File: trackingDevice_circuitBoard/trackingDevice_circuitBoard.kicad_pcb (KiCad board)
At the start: 2 copper layers, 58.4 x 45.7 mm, 15 parts, among them P1 Digital, P4 Analog, Q1 2N7000, Q2 Q_NPN_EBC, Q3 Q_NPN_EBC, U1 HC-12, U2 GY-NEO6MV2, U3 TP4056

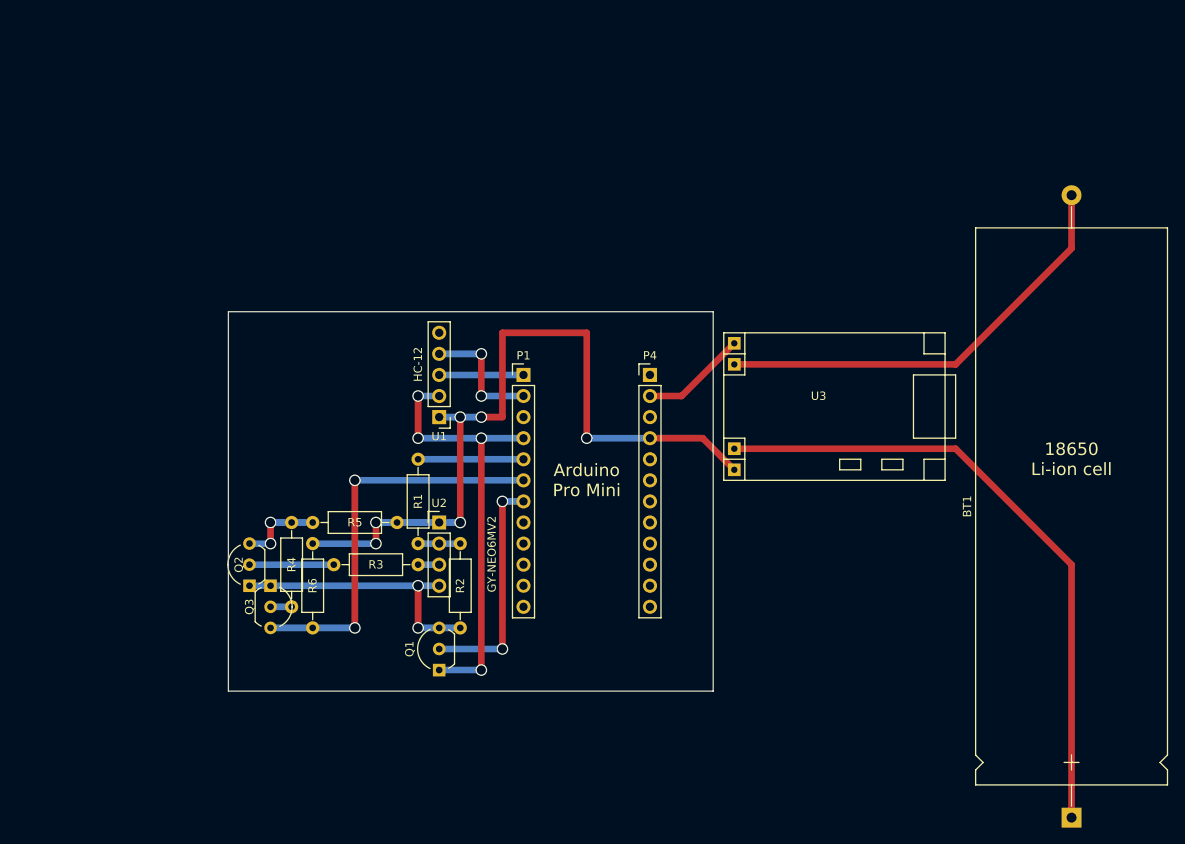
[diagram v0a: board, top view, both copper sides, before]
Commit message: Renamed files and folders
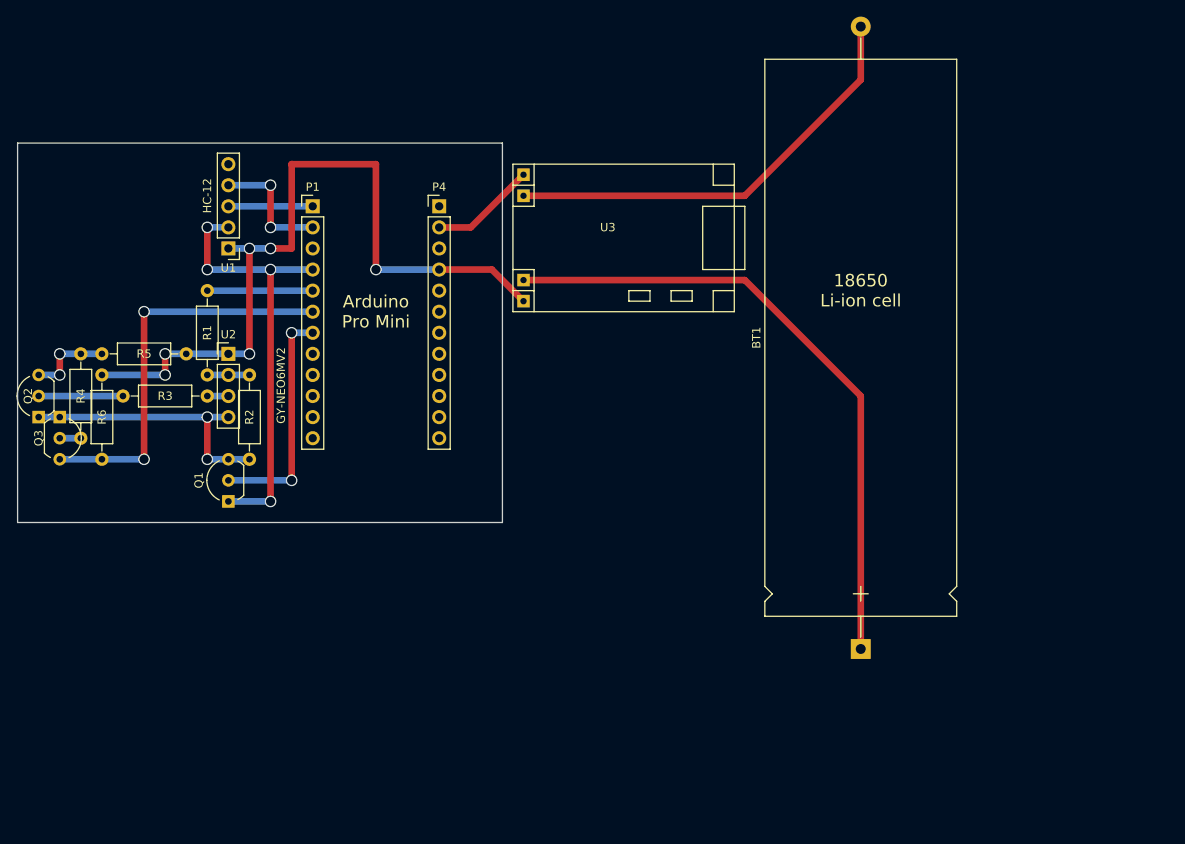
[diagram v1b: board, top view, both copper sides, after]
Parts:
- moved Q1 32.5 mm to (45.7, 78.7)
- moved Q2 32.5 mm to (22.9, 68.6)
- moved Q3 32.5 mm to (25.4, 68.6)
- moved BT1 32.5 mm to (121.9, 96.5)
- moved P1 32.5 mm to (55.9, 43.2)
- moved R4 32.5 mm to (27.9, 71.1)
- moved R5 32.5 mm to (40.6, 61.0)
- moved R6 32.5 mm to (30.5, 63.5)
- moved U1 32.5 mm to (45.7, 48.3)
- moved U2 32.5 mm to (45.7, 61.0)
- moved U3 32.5 mm to (106.7, 55.9)
- moved P4 32.5 mm to (71.1, 43.2)
- moved R1 32.5 mm to (43.2, 53.3)
- moved R2 32.5 mm to (48.3, 63.5)
- moved R3 32.5 mm to (33.0, 66.0)

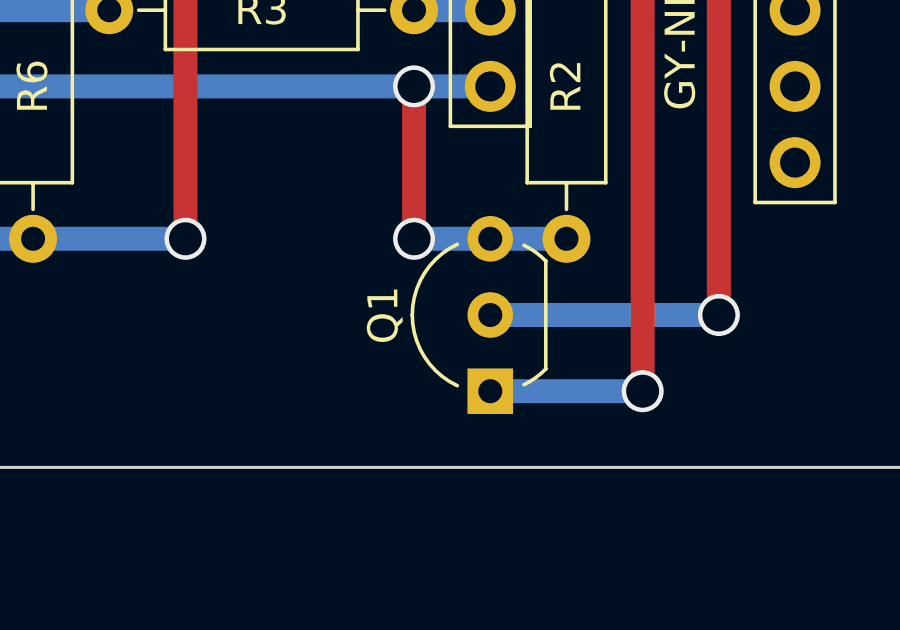
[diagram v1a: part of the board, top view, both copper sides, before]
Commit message: Replaced MOSFET with NPN transistor and changed package to TO-126
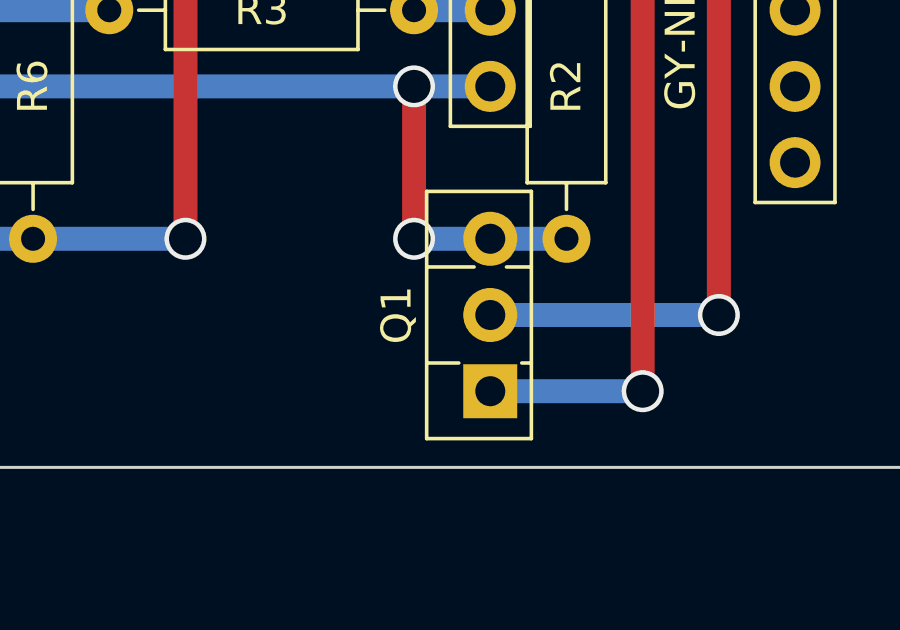
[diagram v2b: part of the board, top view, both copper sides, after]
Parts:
- Q1: value 2N7000 -> Q_NPN_EBC; footprint TO_SOT_Packages_THT:TO-92_Inline_Wide -> TO_SOT_Packages_THT:TO-126_Vertical
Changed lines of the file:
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@@
-(kicad_pcb (version 4) (host pcbnew 4.0.6)
+(kicad_pcb (version 4) (host pcbnew 4.0.7)
   (general
     (links 29)
     (no_connects 2)
-    (area 20.269999 35.509999 78.790001 81.330001)
+    (area 15.535 19.844999 135.555 98.195001)
     (thickness 1.6)
     (drawings 15)
@@
       (outputformat 1)
       (mirror false)
-      (drillshape 1)
+      (drillshape 0)
       (scaleselection 1)
       (outputdirectory ""))
@@
   )
   (module TO_SOT_Packages_THT:TO-92_Inline_Wide (layer F.Cu)
-    (at 45.72 78.74 90)
-    (descr "TO-92 leads in-line, wide, drill 0.8mm (see NXP sot054_po.pdf)")
-    (tags "to-92 sc-43 sc-43a sot54 PA33 transistor")
-    (fp_text reference Q1 (at 2.54 -3.56 270) (layer F.SilkS)
-      (effects (font (size 1 1) (thickness 0.15)))
-    )
-    (fp_text value 2N7000 (at 2.54 -5.08 90) (layer F.Fab)
-      (effects (font (size 1 1) (thickness 0.15)))
-    )
-    (fp_text user %R (at 2.54 -3.56 270) (layer F.Fab)
-      (effects (font (size 1 1) (thickness 0.15)))
-    )
-    (fp_line (start 0.74 1.85) (end 4.34 1.85) (layer F.SilkS) (width 0.12))
-    (fp_line (start 0.8 1.75) (end 4.3 1.75) (layer F.Fab) (width 0.1))
-    (fp_line (start -1.01 -2.73) (end 6.09 -2.73) (layer F.CrtYd) (width 0.05))
-    (fp_line (start -1.01 -2.73) (end -1.01 2.01) (layer F.CrtYd) (width 0.05))
-    (fp_line (start 6.09 2.01) (end 6.09 -2.73) (layer F.CrtYd) (width 0.05))
-    (fp_line (start 6.09 2.01) (end -1.01 2.01) (layer F.CrtYd) (width 0.05))
-    (fp_arc (start 2.54 0) (end 0.74 1.85) (angle 20) (layer F.SilkS) (width 0.12))
-    (fp_arc (start 2.54 0) (end 2.54 -2.6) (angle -65) (layer F.SilkS) (width 0.12))
-    (fp_arc (start 2.54 0) (end 2.54 -2.6) (angle 65) (layer F.SilkS) (width 0.12))
-    (fp_arc (start 2.54 0) (end 2.54 -2.48) (angle 135) (layer F.Fab) (width 0.1))
-    (fp_arc (start 2.54 0) (end 2.54 -2.48) (angle -135) (layer F.Fab) (width 0.1))
-    (fp_arc (start 2.54 0) (end 4.34 1.85) (angle -20) (layer F.SilkS) (width 0.12))
-    (pad 2 thru_hole circle (at 2.54 0 180) (size 1.52 1.52) (drill 0.8) (layers *.Cu *.Mask)
-      (net 7 /4))
-    (pad 3 thru_hole circle (at 5.08 0 180) (size 1.52 1.52) (drill 0.8) (layers *.Cu *.Mask)
-      (net 31 /GPS_GND))
-    (pad 1 thru_hole rect (at 0 0 180) (size 1.52 1.52) (drill 0.8) (layers *.Cu *.Mask)
-      (net 4 GND))
-    (model ${KISYS3DMOD}/TO_SOT_Packages_THT.3dshapes/TO-92_Inline_Wide.wrl
-      (at (xyz 0.1 0 0))
-      (scale (xyz 1 1 1))
-      (rotate (xyz 0 0 -90))
-    )
-  )
-  (module TO_SOT_Packages_THT:TO-92_Inline_Wide (layer F.Cu)
     (at 22.86 68.58 90)
     (descr "TO-92 leads in-line, wide, drill 0.8mm (see NXP sot054_po.pdf)")
@@
     )
   )
+  (module TO_SOT_Packages_THT:TO-126_Vertical (layer F.Cu)
+    (at 45.72 78.74 90)
+    (descr "TO-126, Vertical, RM 2.54mm")
+    (tags "TO-126 Vertical RM 2.54mm")
+    (fp_text reference Q1 (at 2.54 -3.12 90) (layer F.SilkS)
+      (effects (font (size 1 1) (thickness 0.15)))
+    )
+    (fp_text value Q_NPN_EBC (at 2.54 -5.08 90) (layer F.Fab)
+      (effects (font (size 1 1) (thickness 0.15)))
+    )
+    (fp_text user %R (at 2.54 -3.12 90) (layer F.Fab)
+      (effects (font (size 1 1) (thickness 0.15)))
+    )
+    (fp_line (start -1.46 -2) (end -1.46 1.25) (layer F.Fab) (width 0.1))
+    (fp_line (start -1.46 1.25) (end 6.54 1.25) (layer F.Fab) (width 0.1))
+    (fp_line (start 6.54 1.25) (end 6.54 -2) (layer F.Fab) (width 0.1))
+    (fp_line (start 6.54 -2) (end -1.46 -2) (layer F.Fab) (width 0.1))
+    (fp_line (start 0.94 -2) (end 0.94 1.25) (layer F.Fab) (width 0.1))
+    (fp_line (start 4.14 -2) (end 4.14 1.25) (layer F.Fab) (width 0.1))
+    (fp_line (start -1.58 -2.12) (end 6.66 -2.12) (layer F.SilkS) (width 0.12))
+    (fp_line (start -1.58 1.37) (end 6.66 1.37) (layer F.SilkS) (width 0.12))
+    (fp_line (start -1.58 -2.12) (end -1.58 1.37) (layer F.SilkS) (width 0.12))
+    (fp_line (start 6.66 -2.12) (end 6.66 1.37) (layer F.SilkS) (width 0.12))
+    (fp_line (start 0.94 -2.12) (end 0.94 -1.05) (layer F.SilkS) (width 0.12))
+    (fp_line (start 0.94 1.05) (end 0.94 1.37) (layer F.SilkS) (width 0.12))
+    (fp_line (start 4.141 -2.12) (end 4.141 -0.54) (layer F.SilkS) (width 0.12))
+    (fp_line (start 4.141 0.54) (end 4.141 1.37) (layer F.SilkS) (width 0.12))
+    (fp_line (start -1.71 -2.25) (end -1.71 1.5) (layer F.CrtYd) (width 0.05))
+    (fp_line (start -1.71 1.5) (end 6.79 1.5) (layer F.CrtYd) (width 0.05))
+    (fp_line (start 6.79 1.5) (end 6.79 -2.25) (layer F.CrtYd) (width 0.05))
+    (fp_line (start 6.79 -2.25) (end -1.71 -2.25) (layer F.CrtYd) (width 0.05))
+    (pad 1 thru_hole rect (at 0 0 90) (size 1.8 1.8) (drill 1) (layers *.Cu *.Mask)
+      (net 4 GND))
+    (pad 2 thru_hole oval (at 2.54 0 90) (size 1.8 1.8) (drill 1) (layers *.Cu *.Mask)
+      (net 7 /4))
+    (pad 3 thru_hole oval (at 5.08 0 90) (size 1.8 1.8) (drill 1) (layers *.Cu *.Mask)
+      (net 31 /GPS_GND))
+    (model ${KISYS3DMOD}/TO_SOT_Packages_THT.3dshapes/TO-126_Vertical.wrl
+      (at (xyz 0.1 0 0))
+      (scale (xyz 1 1 1))
+      (rotate (xyz 0 0 0))
+    )
+  )
